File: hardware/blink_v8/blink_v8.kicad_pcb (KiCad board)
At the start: 2 copper layers, 119 x 92 mm, 106 parts, among them J1 Conn_01x02, J10 Conn_01x04_Pin, J11 KH-BNC50-3511, J12 KH-BNC50-3511, J13 KH-BNC50-3511, J14 Conn_02x16_Odd_Even, J15 Conn_01x01, J16 Conn_01x01, J2 PJ-320D, J3 PJ-320D, J4 KH-BNC50-3511, J5 Conn_01x04_Pin, J6 Conn_01x04_Pin, J7 Conn_01x06_Pin, J8 Conn_01x06, J9 USB_C_Receptacle, SW1 MK-12C02-G020, SW2 LC1258OASP, SW3 LC1258OASP, SW5 LC1258OASP, U1 AMS1117-3.3, U2 AD8397, U3 M24C02-RMN, U4 STM32F405RGTx, U5 SN74LVC1G14DBV, U6 SN74LVC1G14DBV, U7 CH340C, U8 USBLC6-2P6, U9 MCP73832-2-OT, X1 GTXO-14V (2.048MHz), Y1 16MHz

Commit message: updates
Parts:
- removed J10, J5, J6: Conn_01x04_Pin, Connector_PinHeader_2.54mm:PinHeader_1x04_P2.54mm_Vertical
- removed JP1, JP2, JP3, JP4: SolderJumper_2_Bridged, Jumper:SolderJumper-2_P1.3mm_Bridged_RoundedPad1.0x1.5mm
- added R34: 4K7, Resistor_SMD:R_0603_1608Metric, F.Cu at (213.3, 103.4)
- added R35: 200R, Resistor_SMD:R_0805_2012Metric, F.Cu at (213.2, 88.2)
- added R36: 200R, Resistor_SMD:R_0805_2012Metric, F.Cu at (212.8, 99.0)
- R25: value 4K7 -> 200R; footprint Resistor_SMD:R_0603_1608Metric -> Resistor_SMD:R_0805_2012Metric
- moved R25 6.79 mm to (213.7, 79.3), turned to -90 degrees
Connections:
- J7 pad 3: /DB3 -> /BTN1
- J7 pad 4: /DB2 -> /BOOT1
- J7 pad 5: /DB1 -> /BOOT0
- R25 pad 1: /DB3 -> Net-(R25-Pad1)
- R25 pad 2: Net-(R25-Pad2) -> /BOOT1
- SW2 pad 1: Net-(R25-Pad2) -> Net-(R35-Pad1)
- SW2 pad 2: GND -> +3.3V
- SW3 pad 1: /BTN1 -> Net-(R36-Pad1)
- SW3 pad 2: GND -> +3.3V
- SW5 pad 1: /BOOT1 -> Net-(R25-Pad1)
- U4 pad 56: /DB2 -> /ROW10
- U4 pad 57: /DB1 -> /ROW9
- U7 pad 2: Net-(JP3-B) -> /USB_TX
- U7 pad 3: Net-(JP4-B) -> /USB_RX
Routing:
- net (no net): track 0.00 -> 156.4 mm
- net /DB1: track 85.5 -> 0.00 mm, vias 5 -> 0
- net /DB2: track 70.8 -> 0.00 mm, vias 2 -> 0
- net /DB3: track 110.6 -> 72.9 mm, vias 6 -> 5
- net /USB_RX: track 101.3 -> 116.3 mm
- net Net-(JP4-B): track 15.1 -> 0.00 mm
- net /USB_TX: track 99.8 -> 113.3 mm
- net Net-(JP3-B): track 13.4 -> 0.00 mm
- net Net-(R25-Pad2): track 11.1 -> 0.00 mm
- net Net-(R35-Pad1): track 0.00 -> 9.41 mm
- net Net-(R36-Pad1): track 0.00 -> 8.62 mm
- net /BOOT1: track 58.2 -> 51.1 mm
- net Net-(R25-Pad1): track 0.00 -> 7.01 mm
- net /BTN1: track 92.1 -> 85.2 mm
- net GND: track 1103.2 -> 1107.8 mm
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
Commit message: update v8 blink
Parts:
- moved R14 64.0 mm to (213.2, 91.8), turned to -90 degrees
- moved R18 40.7 mm to (213.6, 82.8), turned to 90 degrees
- moved R31 2.05 mm to (178.6, 96.6)
- moved R32 0.62 mm to (180.0, 100.5)
- moved R7 0.35 mm to (152.5, 64.6), turned to 0 degrees
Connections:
- J14 pad 31: unconnected-(J14-Pin_31-Pad31) -> /AUX_GPS_PPS
- J14 pad 32: unconnected-(J14-Pin_32-Pad32) -> /AUX_CLK
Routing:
- net (no net): track 156.4 -> 0.00 mm
- net /BOOT0: track 49.0 -> 135.2 mm, vias 0 -> 4
- net /BOOT1: track 51.1 -> 124.4 mm, vias 2 -> 4
- net /DB3: track 72.9 -> 0.00 mm, vias 5 -> 0
- net /ROW9: track 14.7 -> 60.2 mm, vias 5 -> 4
- net /ROW10: track 16.1 -> 50.9 mm
- net /AUX_CLK: track 6.36 -> 40.3 mm, vias 0 -> 2
- net GND: track 1107.8 -> 1074.1 mm, vias 43 -> 41
- net /BTN1: track 85.2 -> 111.1 mm, vias 4 -> 5
- net VBUS: track 114.0 -> 96.5 mm
- net /USB_RX: track 116.3 -> 99.8 mm
- net /AUX_GPS_PPS: track 22.7 -> 39.1 mm
- net /USB_TX: track 113.3 -> 98.9 mm, vias 4 -> 2
- net +3.3V: track 452.3 -> 464.2 mm, vias 16 -> 17
- net Net-(U2B-+): track 42.7 -> 31.7 mm
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
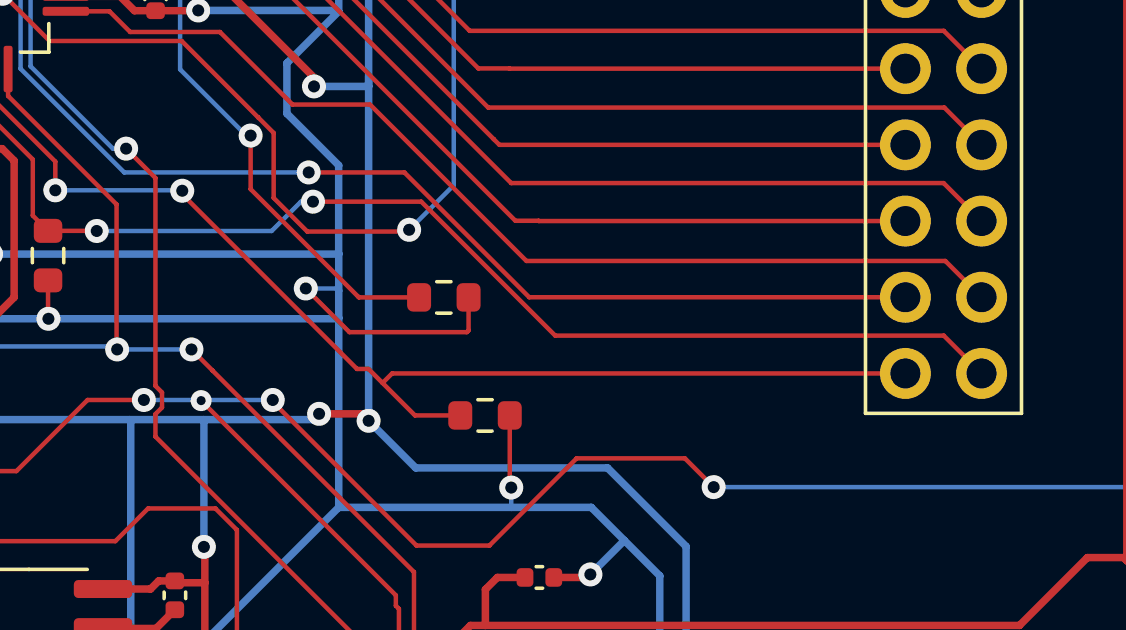
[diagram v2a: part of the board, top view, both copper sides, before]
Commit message: hook up 2 more LED
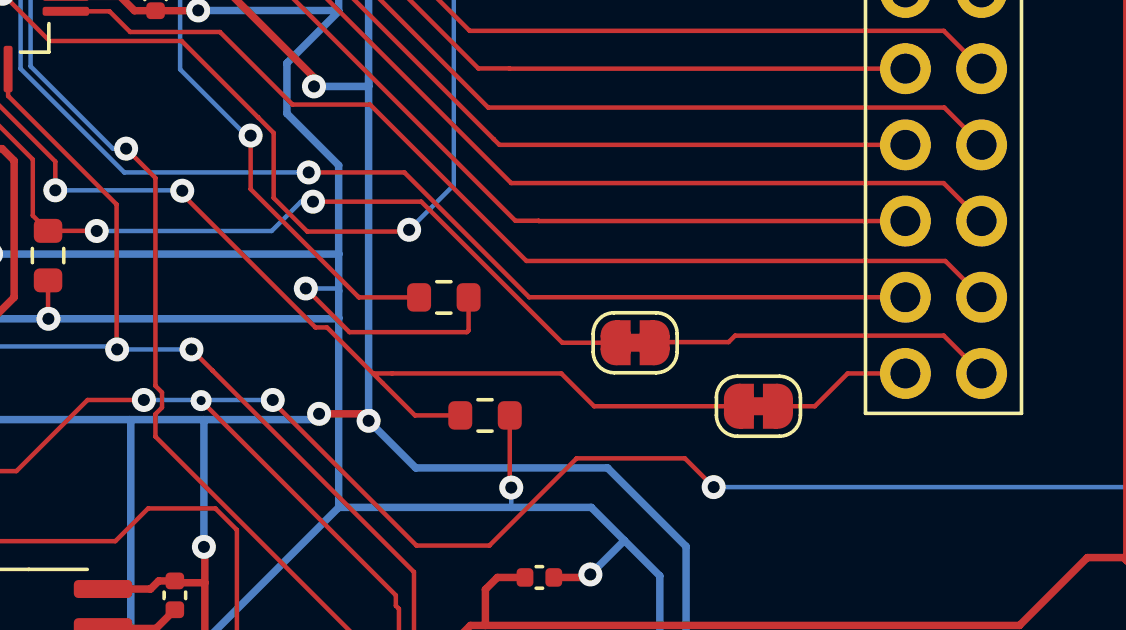
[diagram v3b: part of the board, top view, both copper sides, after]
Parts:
- added JP1: SolderJumper_2_Bridged, Jumper:SolderJumper-2_P1.3mm_Bridged_RoundedPad1.0x1.5mm, F.Cu at (189.1, 100.2)
- added JP2: SolderJumper_2_Bridged, Jumper:SolderJumper-2_P1.3mm_Bridged_RoundedPad1.0x1.5mm, F.Cu at (185.0, 98.1)
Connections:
- J14 pad 31: /AUX_GPS_PPS -> /LEDX
- J14 pad 32: /AUX_CLK -> /LEDY
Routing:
- net /AUX_CLK: track 40.3 -> 27.6 mm
- net /LEDY: track 0.00 -> 11.5 mm
- net /AUX_GPS_PPS: track 39.1 -> 34.2 mm
- net /LEDX: track 0.00 -> 4.70 mm

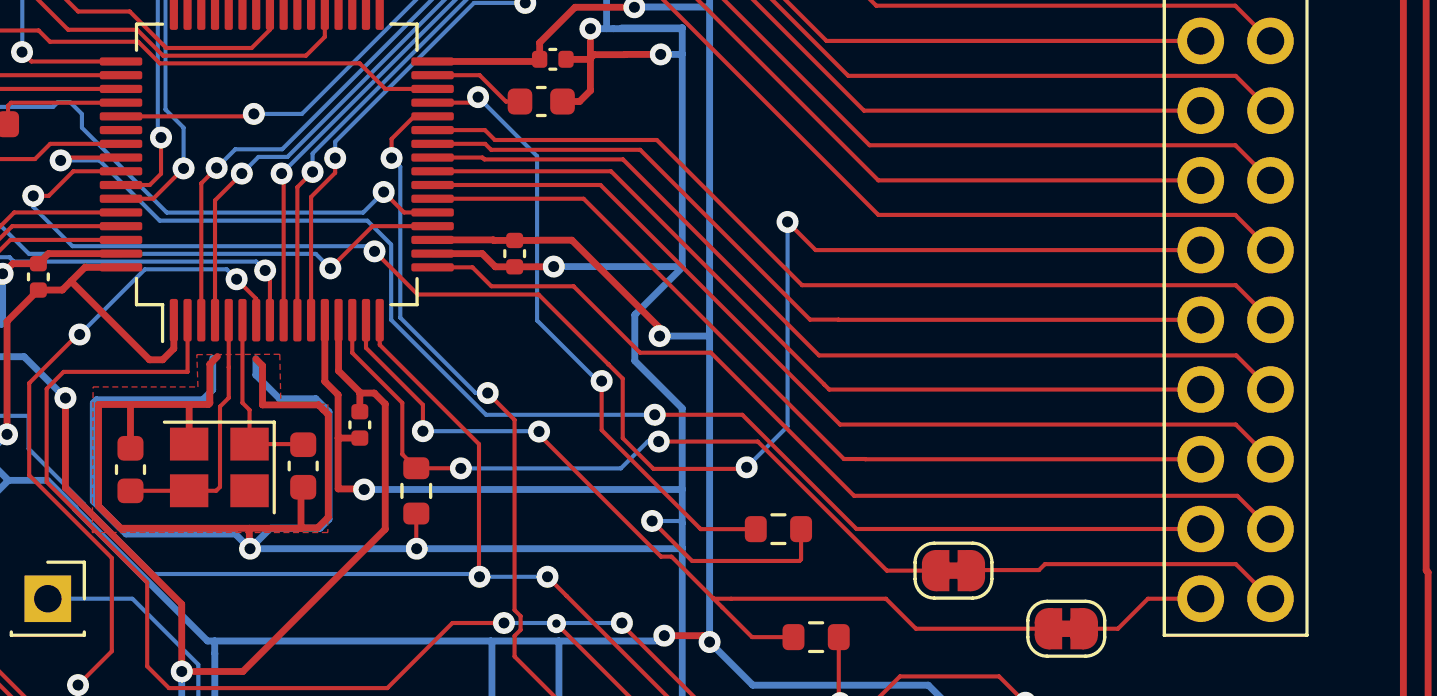
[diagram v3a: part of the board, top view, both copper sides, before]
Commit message: relabel row/col/led
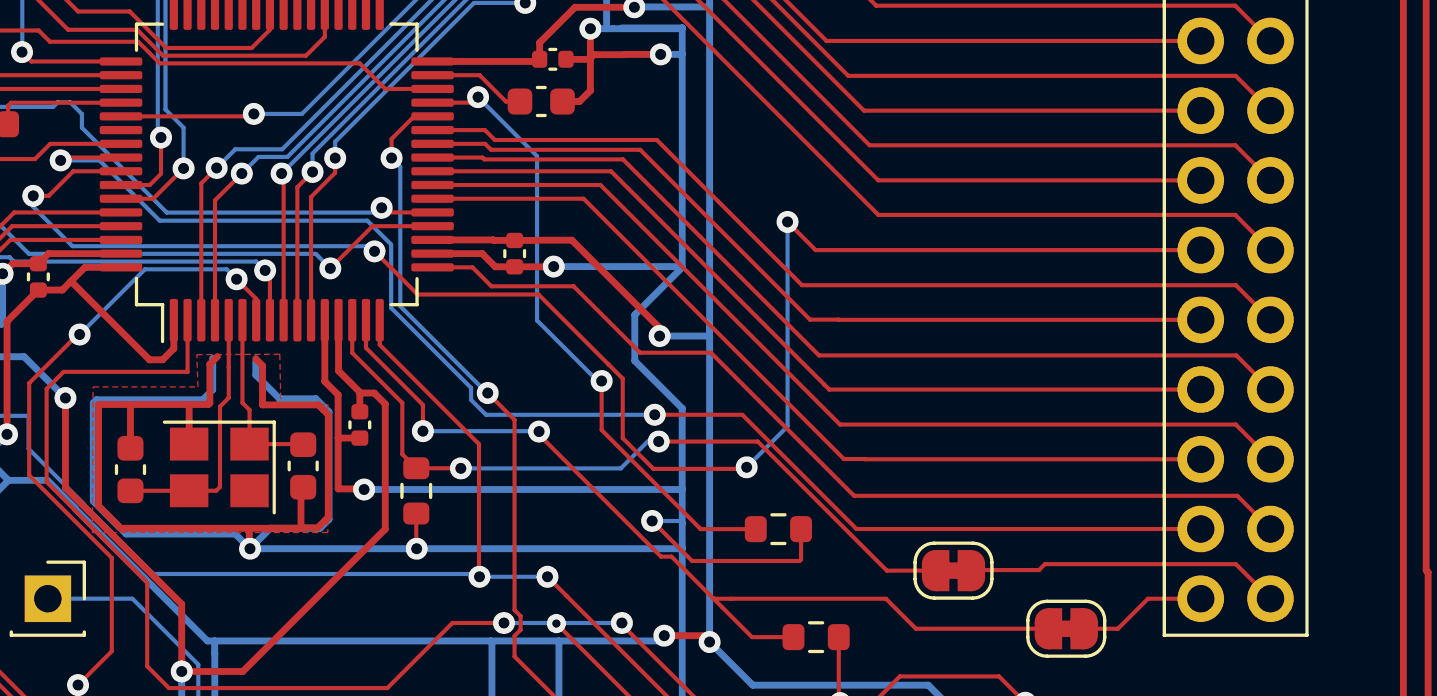
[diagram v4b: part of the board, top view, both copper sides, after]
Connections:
- net /COL1 renamed /LED1
- net /COL2 renamed /LED2
- net /COL3 renamed /LED8
- net /COL4 renamed /LED10
- net /COL5 renamed /LED9
- net /LEDA renamed /NCOL9
- net /LEDB renamed /LEDMR
- net /LEDC renamed /LEDMG
- net /LEDD renamed /LEDMY
- net /LEDE renamed /NCOL1
- net /LEDF renamed /NCOL6
- net /LEDG renamed /NCOL7
- net /LEDH renamed /NCOL8
- net /LEDM1 renamed /NROW1
- net /LEDM2 renamed /LED4
- net /LEDM3 renamed /NCOL10
- net /LEDX renamed /LED5
- net /LEDY renamed /LED6
- net /ROW1 renamed /NCOL2
- net /ROW10 renamed /LED3
- net /ROW2 renamed /NCOL3
- net /ROW3 renamed /NCOL4
- net /ROW4 renamed /NCOL5
- net /ROW5 renamed /LED7
- net /ROW6 renamed /NROW2
- net /ROW7 renamed /NROW3
- net /ROW8 renamed /NROW4
- net /ROW9 renamed /NROW5

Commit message: beter on/off switch
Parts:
- SW1: value MK-12C02-G020 -> SW_SPDT; footprint blinky_footprints:MK-12C02-G025 -> Button_Switch_THT:SW_E-Switch_EG1224_SPDT_Angled
- moved SW1 4.03 mm to (224.0, 120.5)
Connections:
- net /AUX_SYNC_MON renamed /AUX_MON_PPS
- net /SYNC_MON renamed /MON_PPS
- net SYNC_OUT renamed PPS_OUT
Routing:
- net Net-(D2-K): track 41.9 -> 45.0 mm
- net Net-(SW1-B): track 99.4 -> 100.1 mm

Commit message: first sketch of RST/DTR circuit
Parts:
- added JP3: SolderJumper_2_Bridged, Jumper:SolderJumper-2_P1.3mm_Bridged2Bar_RoundedPad1.0x1.5mm, F.Cu at (192.0, 120.4)
- added JP4: SolderJumper_2_Bridged, Jumper:SolderJumper-2_P1.3mm_Bridged2Bar_RoundedPad1.0x1.5mm, F.Cu at (195.6, 120.4)
- added Q1: S8550, Package_TO_SOT_SMD:SC-59, F.Cu at (204.8, 89.6)
- added Q2: S8050, Package_TO_SOT_SMD:SC-59, F.Cu at (204.8, 81.4)
- added R37: 1K0, Resistor_SMD:R_0603_1608Metric, F.Cu at (203.2, 77.7)
- added R38: 1K0, Resistor_SMD:R_0603_1608Metric, F.Cu at (203.4, 85.8)
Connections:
- J7 pad 2: /AUX_MON_PPS -> /BOOT0
- J7 pad 3: /BTN1 -> /BOOT1
- J7 pad 4: /BOOT1 -> /BTN1
- J7 pad 5: /BOOT0 -> /DB3
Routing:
- net Net-(JP3-B): track 0.00 -> 58.6 mm, vias 0 -> 2
- net /DB3: track 0.00 -> 54.3 mm
- net /NRST: track 43.8 -> 86.2 mm, vias 4 -> 6
- net Net-(JP4-B): track 0.00 -> 41.3 mm, vias 0 -> 2
- net /AUX_MON_PPS: track 91.1 -> 57.0 mm, vias 5 -> 4
- net +3.3V: track 464.2 -> 489.7 mm, vias 17 -> 21
- net /USB_DTR: track 0.00 -> 22.7 mm
- net GND: track 1074.1 -> 1089.5 mm, vias 41 -> 42
- net Net-(Q2-B): track 0.00 -> 9.26 mm
- net /USB_RTS: track 0.00 -> 9.18 mm
- net Net-(Q1-B): track 0.00 -> 8.21 mm
- net /BOOT0: track 135.2 -> 142.5 mm, vias 4 -> 5
- net /BOOT1: track 124.2 -> 127.3 mm
- net Net-(SW1-B): track 100.1 -> 99.2 mm
- net VBUS: track 96.5 -> 97.3 mm
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
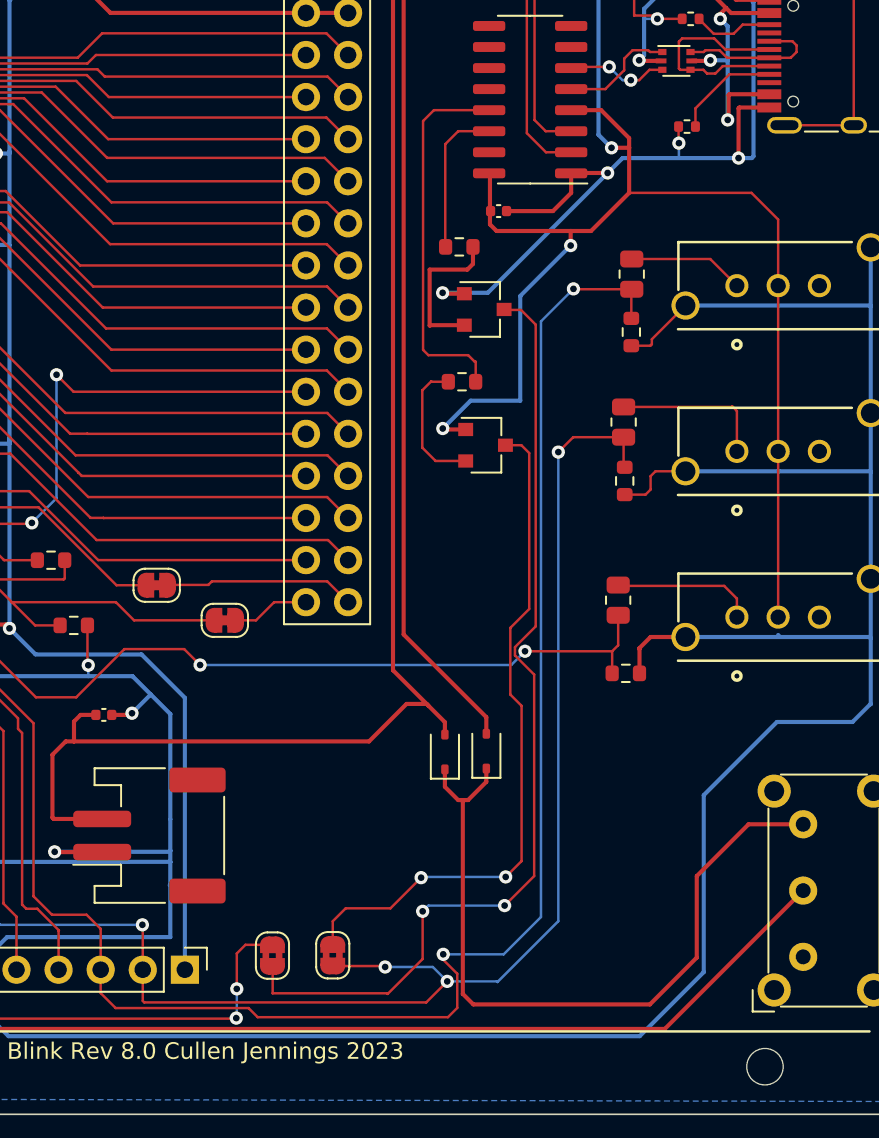
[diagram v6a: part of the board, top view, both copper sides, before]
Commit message: added boot debug connector
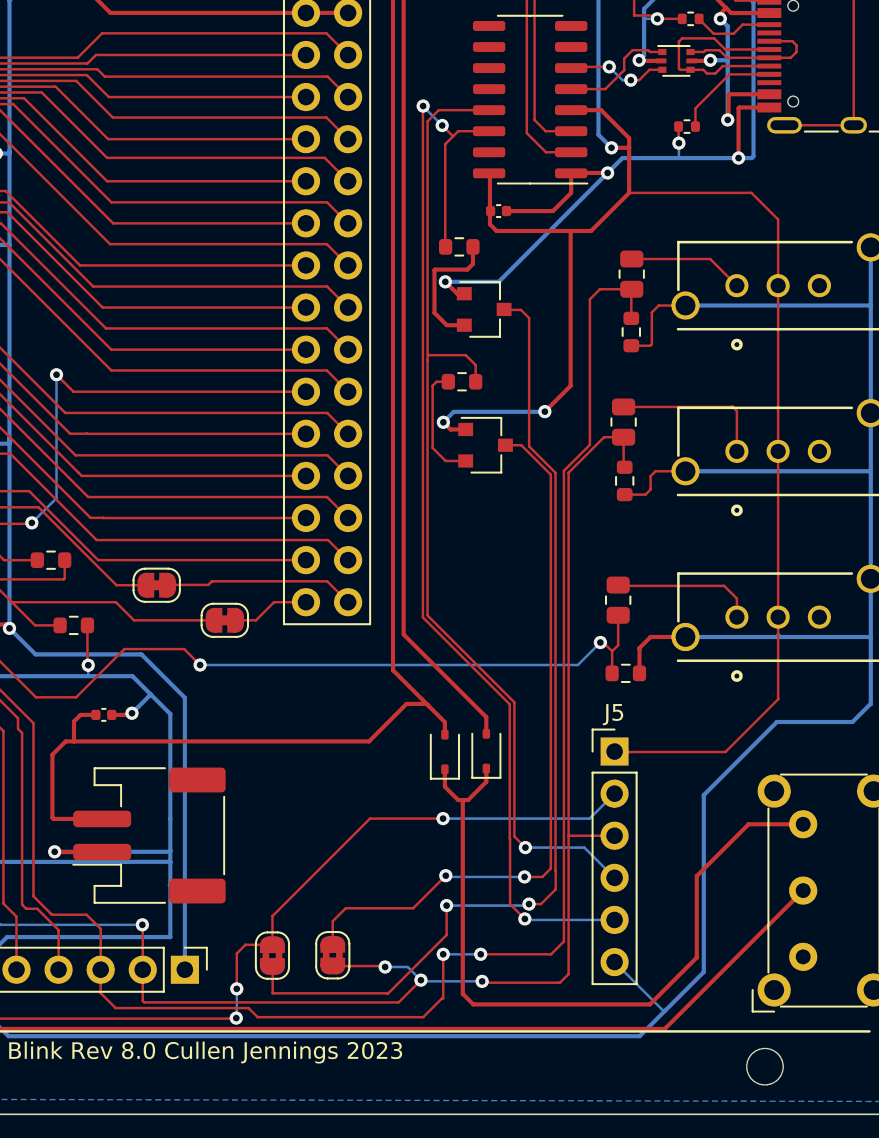
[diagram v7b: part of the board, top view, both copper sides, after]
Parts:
- added J5: Conn_01x06_Pin, Connector_PinHeader_2.54mm:PinHeader_1x06_P2.54mm_Vertical, F.Cu at (212.6, 108.1)
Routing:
- net /USB_RTS: track 9.18 -> 68.8 mm, vias 0 -> 3
- net /USB_DTR: track 22.7 -> 60.5 mm, vias 0 -> 1
- net /NRST: track 86.2 -> 111.7 mm, vias 6 -> 7
- net +3.3V: track 489.7 -> 507.0 mm
- net GND: track 1089.5 -> 1094.4 mm
- net /BOOT0: track 142.5 -> 144.9 mm
- net Net-(JP4-B): track 41.3 -> 43.2 mm
- net Net-(Q1-B): track 8.21 -> 7.12 mm
- net Net-(Q2-B): track 9.26 -> 8.20 mm
- net /BOOT1: track 127.3 -> 126.4 mm
- net Net-(JP3-B): track 58.6 -> 59.2 mm

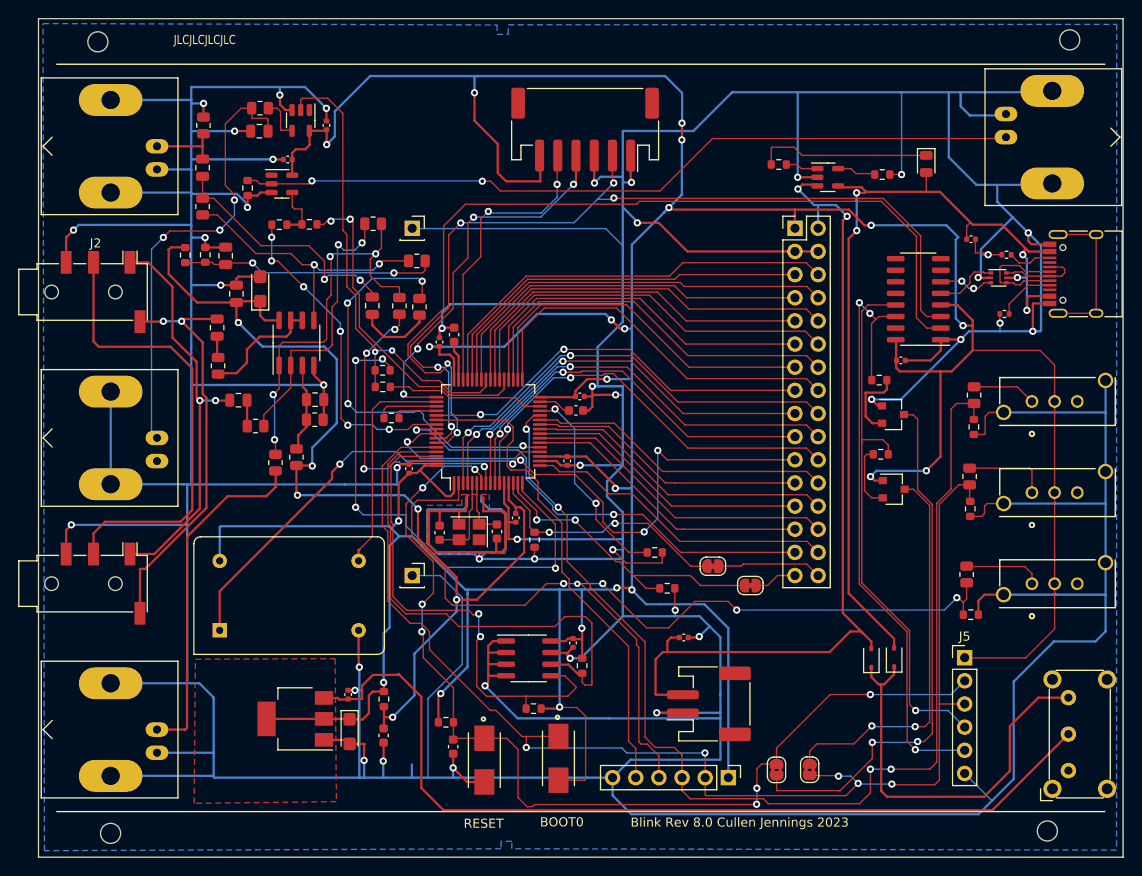
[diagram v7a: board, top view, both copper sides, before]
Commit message: update osc footprint to add mount holes
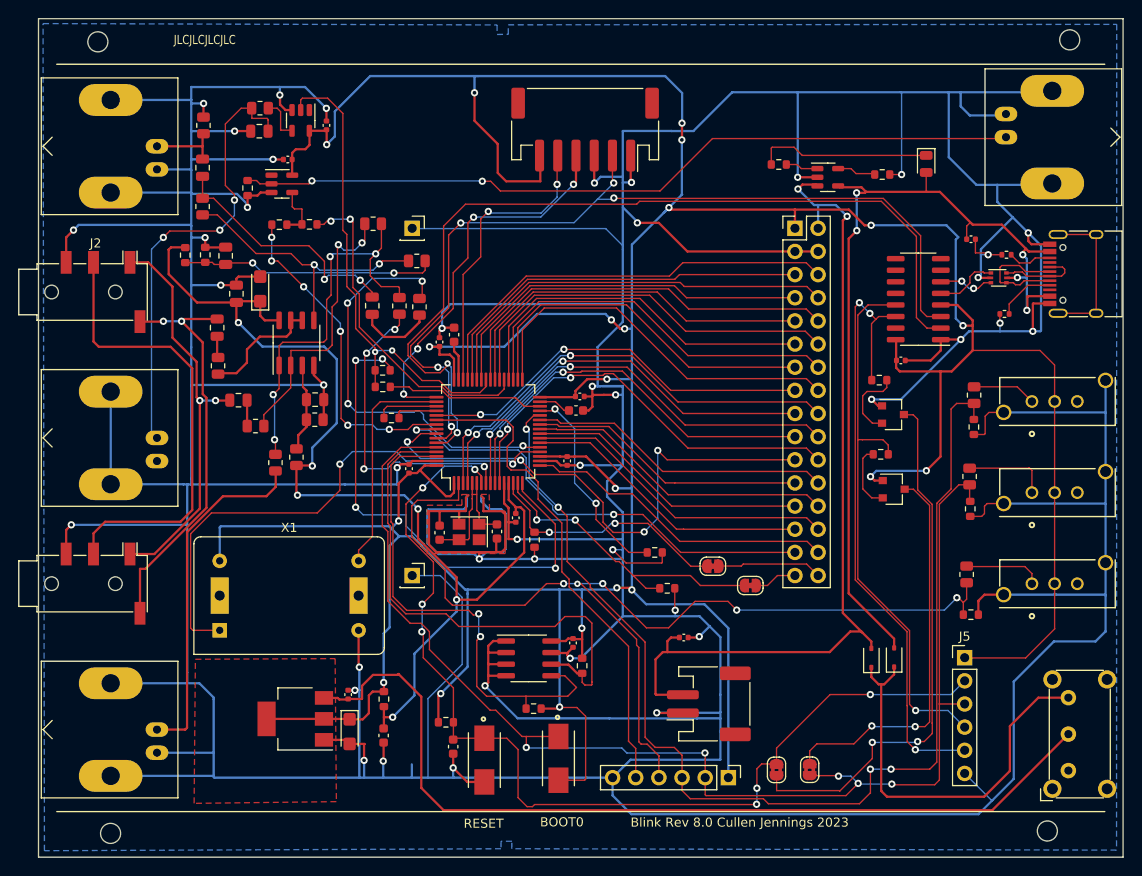
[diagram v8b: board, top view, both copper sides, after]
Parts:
- X1: footprint Oscillator:Oscillator_DIP-14 -> blinky_footprints:Oscillator_DIP-14
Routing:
- net /OSC_ADJ: track 47.6 -> 58.7 mm
- net /USB_DTR: track 60.5 -> 61.4 mm
